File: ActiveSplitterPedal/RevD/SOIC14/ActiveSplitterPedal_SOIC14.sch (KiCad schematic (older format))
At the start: 6 parts, among them J1 MonoJack2Switch, J2 Barrel_Jack, J3 MonoJack2Switch, J4 MonoJack2Switch, J5 MonoJack2Switch, J6 MonoJack2Switch

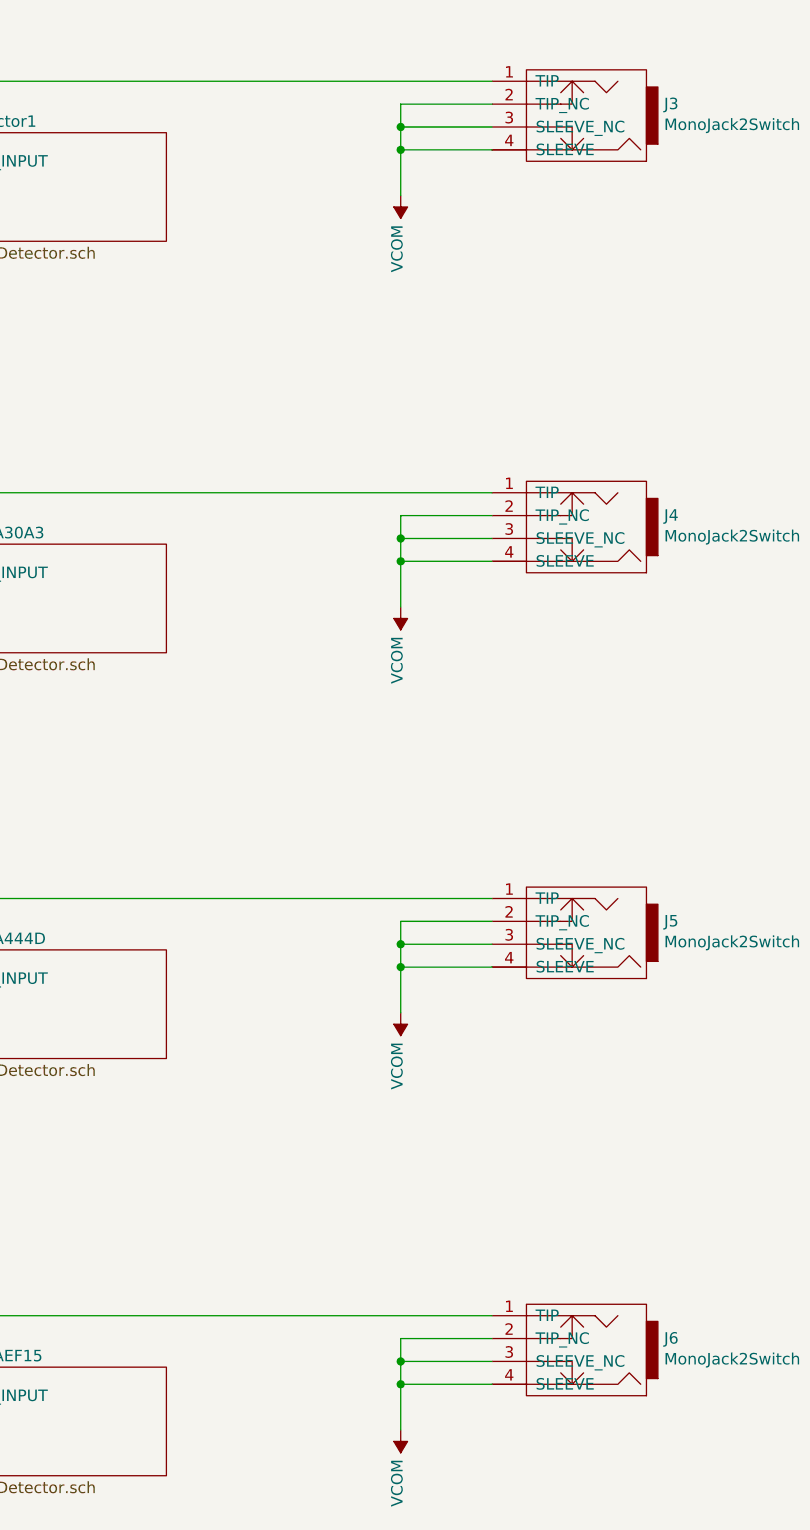
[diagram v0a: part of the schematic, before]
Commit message: updated layout
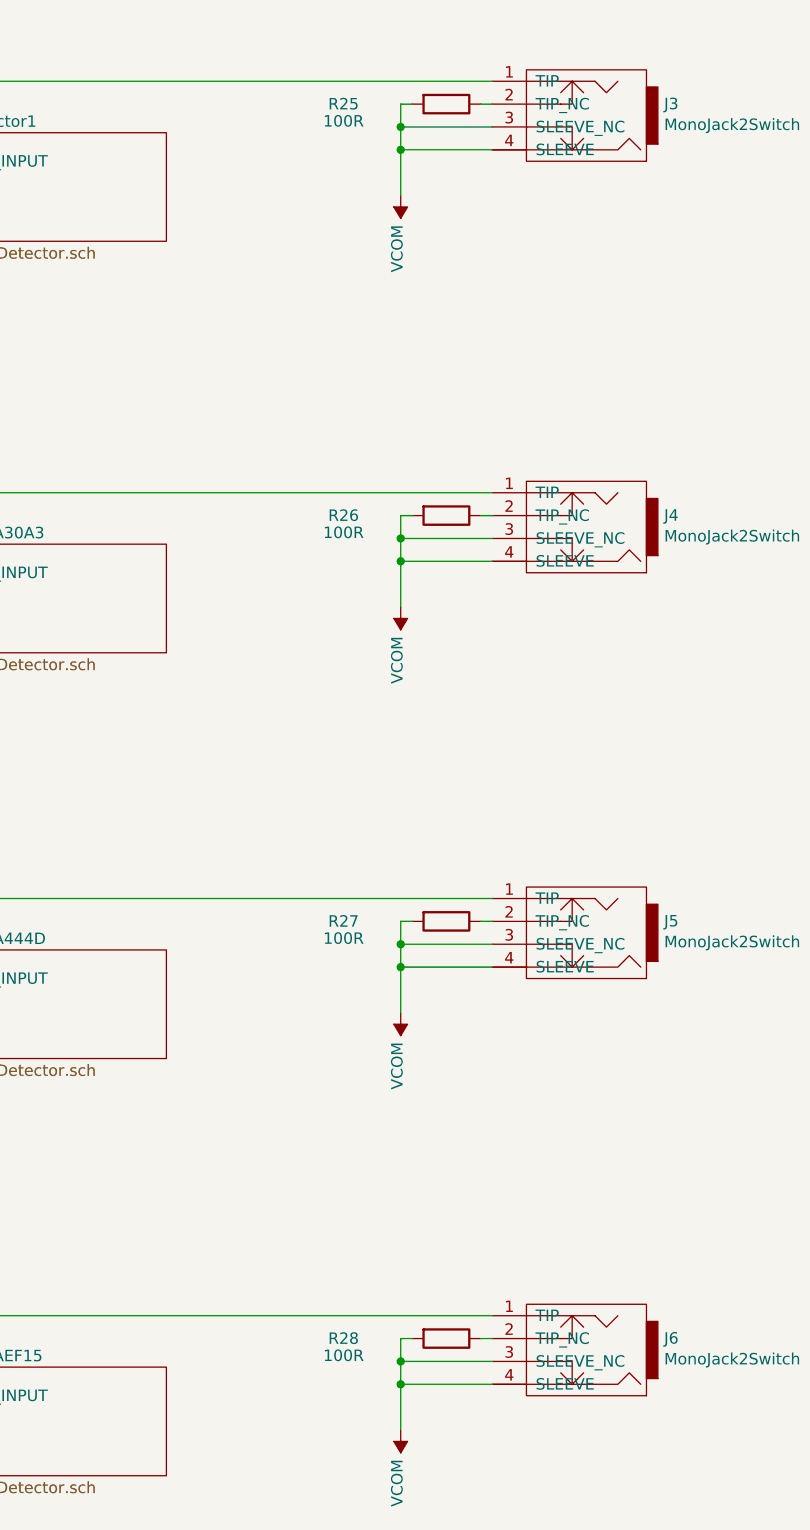
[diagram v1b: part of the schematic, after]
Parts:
- added R25, R26, R27, R28: 100R, Capacitor_SMD:C_0805_2012Metric_Pad1.15x1.40mm_HandSolder, symbol Device:R
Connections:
- net VCOM: now also R25.2, R26.2, R27.2, R28.2; no longer J3.2 (TIP_NC), J4.2 (TIP_NC), J5.2 (TIP_NC), J6.2 (TIP_NC)
- new net: J3.2 (TIP_NC), R25.1
- new net: J4.2 (TIP_NC), R26.1
- new net: J5.2 (TIP_NC), R27.1
- new net: J6.2 (TIP_NC), R28.1
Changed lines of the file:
@@
 	10900 7100 10900 7200
 Wire Wire Line
-	11300 7100 10900 7100
+	11300 7100 11250 7100
 Wire Wire Line
 	10900 5475 10900 5675
@@
 	10900 5275 10900 5375
 Wire Wire Line
-	11300 5275 10900 5275
+	11300 5275 11250 5275
 Wire Wire Line
 	10900 3700 10900 3900
@@
 	10900 3500 10900 3600
 Wire Wire Line
-	11300 3500 10900 3500
+	11300 3500 11250 3500
 Wire Wire Line
 	10900 1900 10900 2100
@@
 	10900 1700 10900 1800
 Wire Wire Line
-	11300 1700 10900 1700
+	11300 1700 11250 1700
 Wire Wire Line
 	3450 1900 3450 2375
@@
 	-1   0    0    1
 $EndComp
+$Comp
+L Device:R R25
+U 1 1 5F62BA16
+P 11100 1700
+F 0 "R25" V 11100 1250 50  0000 C CNN
+F 1 "100R" V 11175 1250 50  0000 C CNN
+F 2 "Capacitor_SMD:C_0805_2012Metric_Pad1.15x1.40mm_HandSolder" V 11030 1700 50  0001 C CNN
+F 3 "~" H 11100 1700 50  0001 C CNN
+	1    11100 1700
+	0    1    1    0
+$EndComp
+Wire Wire Line
+	10950 1700 10900 1700
+$Comp
+L Device:R R26
+U 1 1 5F62C4AF
+P 11100 3500
+F 0 "R26" V 11100 3050 50  0000 C CNN
+F 1 "100R" V 11175 3050 50  0000 C CNN
+F 2 "Capacitor_SMD:C_0805_2012Metric_Pad1.15x1.40mm_HandSolder" V 11030 3500 50  0001 C CNN
+F 3 "~" H 11100 3500 50  0001 C CNN
+	1    11100 3500
+	0    1    1    0
+$EndComp
+Wire Wire Line
+	10950 3500 10900 3500
+$Comp
+L Device:R R27
+U 1 1 5F62CF86
+P 11100 5275
+F 0 "R27" V 11100 4825 50  0000 C CNN
+F 1 "100R" V 11175 4825 50  0000 C CNN
+F 2 "Capacitor_SMD:C_0805_2012Metric_Pad1.15x1.40mm_HandSolder" V 11030 5275 50  0001 C CNN
+F 3 "~" H 11100 5275 50  0001 C CNN
+	1    11100 5275
+	0    1    1    0
+$EndComp
+Wire Wire Line
+	10950 5275 10900 5275
+$Comp
+L Device:R R28
+U 1 1 5F62D6CF
+P 11100 7100
+F 0 "R28" V 11100 6650 50  0000 C CNN
+F 1 "100R" V 11175 6650 50  0000 C CNN
+F 2 "Capacitor_SMD:C_0805_2012Metric_Pad1.15x1.40mm_HandSolder" V 11030 7100 50  0001 C CNN
+F 3 "~" H 11100 7100 50  0001 C CNN
+	1    11100 7100
+	0    1    1    0
+$EndComp
+Wire Wire Line
+	10950 7100 10900 7100
 $EndSCHEMATC
